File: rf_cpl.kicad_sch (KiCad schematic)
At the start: 4 parts, among them J3 N_PAD, U10 GAT-30+, U8 GAT-30+, U9 SYBD-30-62HP+

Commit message: pcb update
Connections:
- net CPL_FWD: now reaches U10.1 (In), U9.3 (Rev)
- net RF_OUT_CONN: now reaches J3.1 (In), U9.1 (In)
- net CPL_REF: now reaches U8.1 (In), U9.4 (Fwd)
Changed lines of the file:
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@@
   (title_block
     (title "M17 Remote Radio Unit - RF board")
-    (date "15-10-2023")
+    (date "27-10-2023")
     (rev "A")
     (company "M17 Project")
@@
     (effects (font (size 1.27 1.27)) (justify left bottom))
   )
+  (label "RF_OUT_CONN" (at 222.25 129.54 0) (fields_autoplaced)
+    (effects (font (size 1.27 1.27)) (justify left bottom))
+  )
+  (label "CPL_REF" (at 193.04 139.7 0) (fields_autoplaced)
+    (effects (font (size 1.27 1.27)) (justify left bottom))
+  )
+  (label "CPL_FWD" (at 223.52 139.7 0) (fields_autoplaced)
+    (effects (font (size 1.27 1.27)) (justify left bottom))
+  )

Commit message: date update
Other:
- title: M17 Remote Radio Unit - RF board -> Remote Radio Unit - RF board
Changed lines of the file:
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@@
   (paper "A3")
   (title_block
-    (title "M17 Remote Radio Unit - RF board")
-    (date "28-10-2023")
+    (title "Remote Radio Unit - RF board")
+    (date "30-10-2023")
     (rev "A")
     (company "M17 Project")

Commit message: MPN/PN update
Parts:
- J3, U10, U8, U9: MPN (none) -> -
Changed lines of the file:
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@@
+      (effects (font (size 1.27 1.27)) hide)
+    )
+    (property "MPN" "-" (at 223.52 151.13 0)
       (effects (font (size 1.27 1.27)) hide)
     )
@@
       (effects (font (size 1.27 1.27)) hide)
     )
+    (property "MPN" "-" (at 242.57 129.54 0)
+      (effects (font (size 1.27 1.27)) hide)
+    )
     (pin "1")
     (pin "2")
@@
     )
     (property "PN" "-" (at 193.04 151.13 0)
+      (effects (font (size 1.27 1.27)) hide)
+    )
+    (property "MPN" "-" (at 193.04 151.13 0)
       (effects (font (size 1.27 1.27)) hide)
     )
@@
       (effects (font (size 1.27 1.27)) hide)
     )
+    (property "MPN" "-" (at 208.28 127 0)
+      (effects (font (size 1.27 1.27)) hide)
+    )

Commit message: attenuators' PN update
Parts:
- U10, U8: MPN - -> 139-GAT-30+; PN - -> 139-GAT-30+
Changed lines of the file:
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@@
   (title_block
     (title "Remote Radio Unit - RF board")
-    (date "03-11-2023")
+    (date "10-11-2023")
     (rev "A")
     (company "M17 Project")
@@
       (effects (font (size 1.27 1.27)) hide)
     )
-    (property "PN" "-" (at 223.52 151.13 0)
-      (effects (font (size 1.27 1.27)) hide)
-    )
-    (property "MPN" "-" (at 223.52 151.13 0)
+    (property "PN" "139-GAT-30+" (at 223.52 151.13 0)
+      (effects (font (size 1.27 1.27)) hide)
+    )
+    (property "MPN" "139-GAT-30+" (at 223.52 151.13 0)
       (effects (font (size 1.27 1.27)) hide)
     )
@@
       (effects (font (size 1.27 1.27)) hide)
     )
-    (property "PN" "-" (at 193.04 151.13 0)
-      (effects (font (size 1.27 1.27)) hide)
-    )
-    (property "MPN" "-" (at 193.04 151.13 0)
-      (effects (font (size 1.27 1.27)) hide)
-    )
+    (property "PN" "139-GAT-30+" (at 193.04 151.13 0)
+      (effects (font (size 1.27 1.27)) hide)
+    )
+    (property "MPN" "139-GAT-30+" (at 193.04 151.13 0)
+      (effects (font (size 1.27 1.27)) hide)
+    )

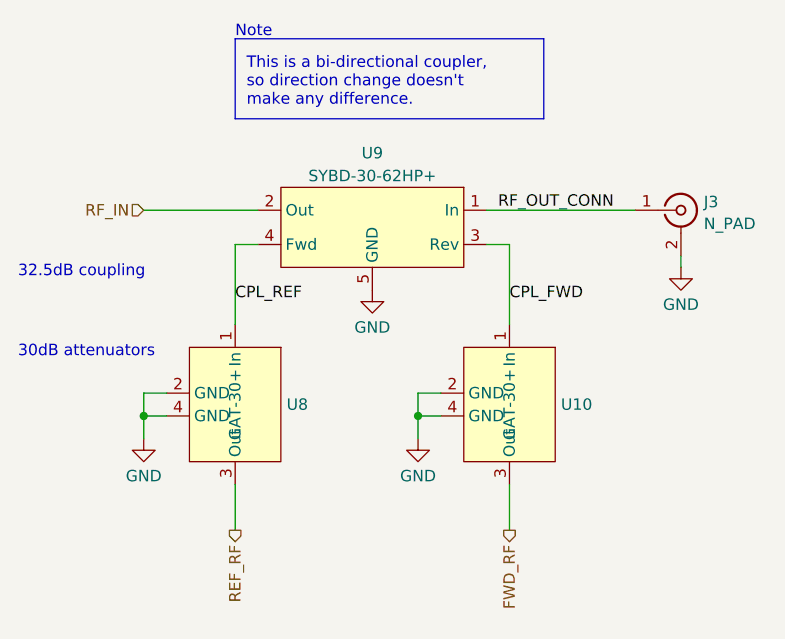
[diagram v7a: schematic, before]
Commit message: WIP rev B
- replaced R44-R46 with 22k
- exposed BOOT0 at the DA15 connector
- added a testpoint at DAC OUT2
- added a buffer to the 40MHz reference oscillator
- removed C2
- bypassed R5 with a 100nF capacitor
- changed D5's voltage to 5.1V
- routed TX_SAMP_CLK
- changed temperature sensor's supply voltage to 5V
- added a series of 100p, 1n and 10n capacitors at PA_VGG
- reduced N-connector cutouts to 2.5mm
- improved RF output track a little
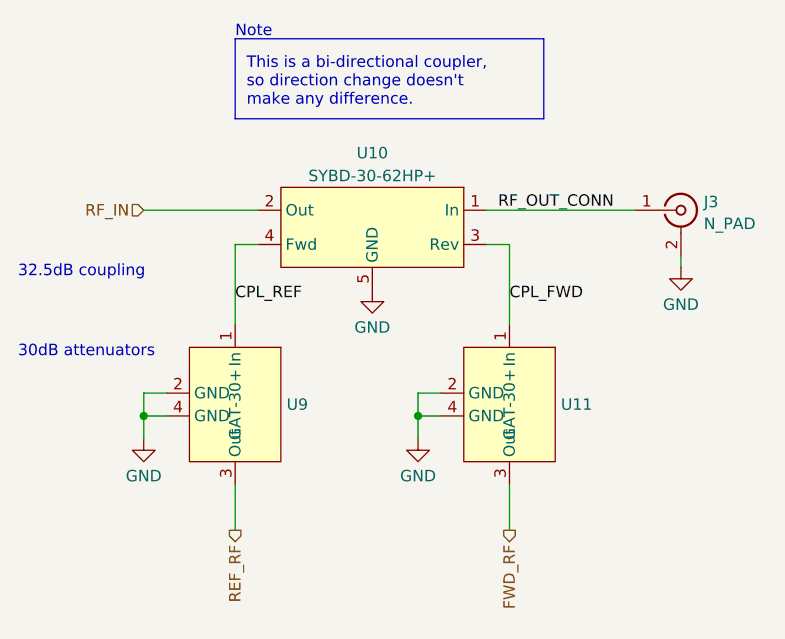
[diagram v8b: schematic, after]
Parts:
- renumbered U9 to U10, U10 to U11, U8 to U9
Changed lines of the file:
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@@
   (title_block
     (title "Remote Radio Unit - RF board")
-    (date "10-11-2023")
-    (rev "A")
+    (date "18-01-2024")
+    (rev "B")
     (company "M17 Project")
     (comment 1 "Wojciech Kaczmarski, SP5WWP")
@@
   (symbol (lib_id "power:GND") (at 182.88 154.94 0) (unit 1)
     (in_bom yes) (on_board yes) (dnp no) (fields_autoplaced)
-    (property "Reference" "#PWR056" (at 182.88 161.29 0)
+    (property "Reference" "#PWR062" (at 182.88 161.29 0)
       (effects (font (size 1.27 1.27)) hide)
     )
@@
       (project "m17-rru-rf"
         (path "/4c42207c-9e6b-42da-ad38-da126b892014/59b2721c-5b8a-4fc3-bf5e-590dec787afb"
-          (reference "#PWR056") (unit 1)
+          (reference "#PWR062") (unit 1)
         )
       )
@@
   (symbol (lib_id "power:GND") (at 242.57 135.89 0) (unit 1)
     (in_bom yes) (on_board yes) (dnp no) (fields_autoplaced)
-    (property "Reference" "#PWR059" (at 242.57 142.24 0)
+    (property "Reference" "#PWR065" (at 242.57 142.24 0)
       (effects (font (size 1.27 1.27)) hide)
     )
@@
       (project "m17-rru-rf"
         (path "/4c42207c-9e6b-42da-ad38-da126b892014/59b2721c-5b8a-4fc3-bf5e-590dec787afb"
-          (reference "#PWR059") (unit 1)
+          (reference "#PWR065") (unit 1)
         )
       )
@@
   (symbol (lib_id "Parts:GAT-30+") (at 223.52 151.13 270) (unit 1)
     (in_bom yes) (on_board yes) (dnp no) (fields_autoplaced)
-    (property "Reference" "U10" (at 229.235 151.13 90)
+    (property "Reference" "U11" (at 229.235 151.13 90)
       (effects (font (size 1.27 1.27)) (justify left))
     )
@@
       (project "m17-rru-rf"
         (path "/4c42207c-9e6b-42da-ad38-da126b892014/59b2721c-5b8a-4fc3-bf5e-590dec787afb"
-          (reference "U10") (unit 1)
+          (reference "U11") (unit 1)
         )
       )
@@
   (symbol (lib_id "Parts:GAT-30+") (at 193.04 151.13 270) (unit 1)
     (in_bom yes) (on_board yes) (dnp no) (fields_autoplaced)
-    (property "Reference" "U8" (at 198.755 151.13 90)
+    (property "Reference" "U9" (at 198.755 151.13 90)
       (effects (font (size 1.27 1.27)) (justify left))
     )
@@
       (project "m17-rru-rf"
         (path "/4c42207c-9e6b-42da-ad38-da126b892014/59b2721c-5b8a-4fc3-bf5e-590dec787afb"
-          (reference "U8") (unit 1)
+          (reference "U9") (unit 1)
         )
       )
@@
   (symbol (lib_id "Parts:SYBD-30-62HP+") (at 208.28 127 0) (mirror y) (unit 1)
     (in_bom yes) (on_board yes) (dnp no)
-    (property "Reference" "U9" (at 208.28 123.19 0)
+    (property "Reference" "U10" (at 208.28 123.19 0)
       (effects (font (size 1.27 1.27)))
     )
@@
       (project "m17-rru-rf"
         (path "/4c42207c-9e6b-42da-ad38-da126b892014/59b2721c-5b8a-4fc3-bf5e-590dec787afb"
-          (reference "U9") (unit 1)
+          (reference "U10") (unit 1)
         )
       )
@@
   (symbol (lib_id "power:GND") (at 208.28 138.43 0) (unit 1)
     (in_bom yes) (on_board yes) (dnp no) (fields_autoplaced)
-    (property "Reference" "#PWR057" (at 208.28 144.78 0)
+    (property "Reference" "#PWR063" (at 208.28 144.78 0)
       (effects (font (size 1.27 1.27)) hide)
     )
@@
       (project "m17-rru-rf"
         (path "/4c42207c-9e6b-42da-ad38-da126b892014/59b2721c-5b8a-4fc3-bf5e-590dec787afb"
-          (reference "#PWR057") (unit 1)
+          (reference "#PWR063") (unit 1)
         )
       )
@@
   (symbol (lib_id "power:GND") (at 213.36 154.94 0) (unit 1)
     (in_bom yes) (on_board yes) (dnp no) (fields_autoplaced)
-    (property "Reference" "#PWR058" (at 213.36 161.29 0)
+    (property "Reference" "#PWR064" (at 213.36 161.29 0)
       (effects (font (size 1.27 1.27)) hide)
     )
@@
       (project "m17-rru-rf"
         (path "/4c42207c-9e6b-42da-ad38-da126b892014/59b2721c-5b8a-4fc3-bf5e-590dec787afb"
-          (reference "#PWR058") (unit 1)
-        )
-      )
+          (reference "#PWR064") (unit 1)
+        )
+      )
